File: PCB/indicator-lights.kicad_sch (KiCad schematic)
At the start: 10 parts, among them IC9 IS31FL3218-GRLS2

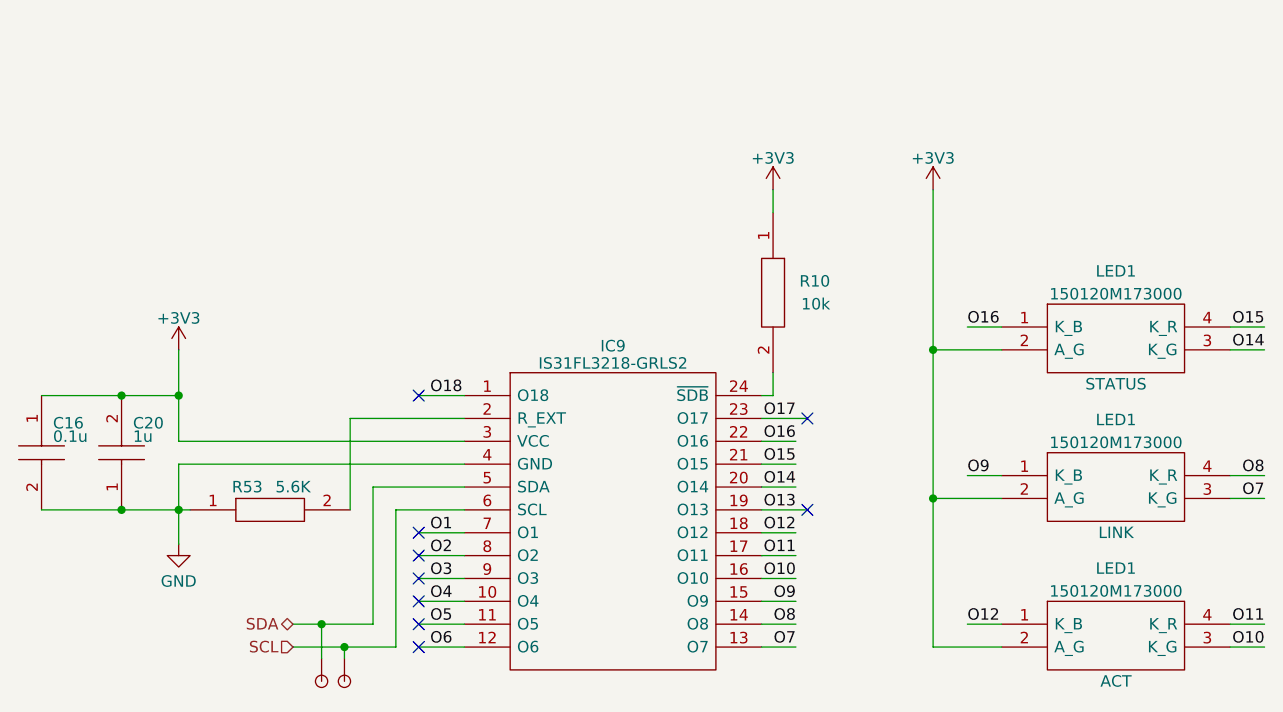
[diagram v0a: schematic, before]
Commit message: preliminary routing completed
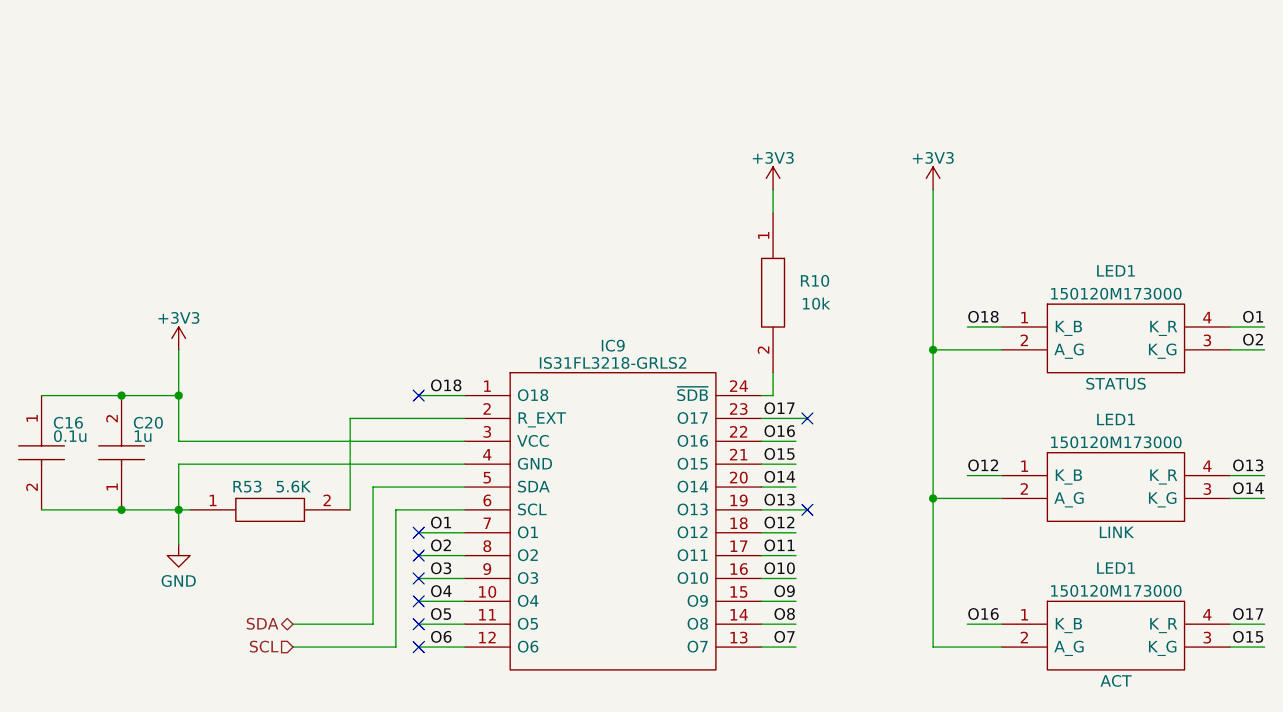
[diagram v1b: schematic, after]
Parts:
- removed DBG5 (x2): ~, Oro Footprints:DebugPin, symbol Oro:DebugPin
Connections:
- net O1: now also LED1.4 (K_R)
- net O10: no longer LED1.3 (K_G)
- net O11: no longer LED1.4 (K_R)
- net O12: now also LED1.1 (K_B); no longer LED1.1 (K_B)
- net O13: now also LED1.4 (K_R)
- net O14: now also LED1.3 (K_G); no longer LED1.3 (K_G)
- net O15: now also LED1.3 (K_G); no longer LED1.4 (K_R)
- net O16: now also LED1.1 (K_B); no longer LED1.1 (K_B)
- net O17: now also LED1.4 (K_R)
- net O18: now also LED1.1 (K_B)
- net O2: now also LED1.3 (K_G)
- net O7: no longer LED1.3 (K_G)
- net O8: no longer LED1.4 (K_R)
- net O9: no longer LED1.1 (K_B)
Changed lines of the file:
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@@
   (junction (at 87.63 96.52) (diameter 0) (color 0 0 0 0)
   )
-  (junction (at 103.505 121.92) (diameter 0) (color 0 0 0 0)
-  )
   (junction (at 81.28 109.22) (diameter 0) (color 0 0 0 0)
   )
   (junction (at 171.45 91.44) (diameter 0) (color 0 0 0 0)
-  )
-  (junction (at 106.045 124.46) (diameter 0) (color 0 0 0 0)
   )
   (junction (at 87.63 109.22) (diameter 0) (color 0 0 0 0)
@@
     (stroke (width 0) (type default))
   )
-  (wire (pts (xy 100.33 121.92) (xy 103.505 121.92))
+  (wire (pts (xy 100.33 121.92) (xy 109.22 121.92))
     (stroke (width 0) (type default))
   )
@@
     (stroke (width 0) (type default))
   )
-  (wire (pts (xy 103.505 121.92) (xy 109.22 121.92))
-    (stroke (width 0) (type default))
-  )
   (wire (pts (xy 208.28 124.46) (xy 204.47 124.46))
     (stroke (width 0) (type default))
@@
     (stroke (width 0) (type default))
   )
-  (wire (pts (xy 103.505 121.92) (xy 103.505 125.73))
-    (stroke (width 0) (type default))
-  )
   (wire (pts (xy 156.21 119.38) (xy 152.4 119.38))
     (stroke (width 0) (type default))
@@
     (stroke (width 0) (type default))
   )
-  (wire (pts (xy 106.045 124.46) (xy 111.76 124.46))
-    (stroke (width 0) (type default))
-  )
   (wire (pts (xy 114.3 111.76) (xy 119.38 111.76))
     (stroke (width 0) (type default))
@@
     (stroke (width 0) (type default))
   )
-  (wire (pts (xy 106.045 124.46) (xy 106.045 125.73))
-    (stroke (width 0) (type default))
-  )
   (wire (pts (xy 72.39 109.22) (xy 81.28 109.22))
     (stroke (width 0) (type default))
@@
     (stroke (width 0) (type default))
   )
-  (wire (pts (xy 100.33 124.46) (xy 106.045 124.46))
+  (wire (pts (xy 100.33 124.46) (xy 111.76 124.46))
     (stroke (width 0) (type default))
   )
@@
     (effects (font (size 1.27 1.27)) (justify left bottom))
   )
-  (label "O14" (at 208.28 91.44 180) (fields_autoplaced)
-    (effects (font (size 1.27 1.27)) (justify right bottom))
-  )
-  (label "O16" (at 175.26 88.9 0) (fields_autoplaced)
+  (label "O2" (at 208.28 91.44 180) (fields_autoplaced)
+    (effects (font (size 1.27 1.27)) (justify right bottom))
+  )
+  (label "O18" (at 175.26 88.9 0) (fields_autoplaced)
     (effects (font (size 1.27 1.27)) (justify left bottom))
   )
@@
     (effects (font (size 1.27 1.27)) (justify left bottom))
   )
-  (label "O15" (at 208.28 88.9 180) (fields_autoplaced)
+  (label "O1" (at 208.28 88.9 180) (fields_autoplaced)
     (effects (font (size 1.27 1.27)) (justify right bottom))
   )
@@
     (effects (font (size 1.27 1.27)) (justify left bottom))
   )
-  (label "O11" (at 208.28 121.92 180) (fields_autoplaced)
-    (effects (font (size 1.27 1.27)) (justify right bottom))
-  )
-  (label "O12" (at 175.26 121.92 0) (fields_autoplaced)
-    (effects (font (size 1.27 1.27)) (justify left bottom))
-  )
-  (label "O10" (at 208.28 124.46 180) (fields_autoplaced)
+  (label "O17" (at 208.28 121.92 180) (fields_autoplaced)
+    (effects (font (size 1.27 1.27)) (justify right bottom))
+  )
+  (label "O16" (at 175.26 121.92 0) (fields_autoplaced)
+    (effects (font (size 1.27 1.27)) (justify left bottom))
+  )
+  (label "O15" (at 208.28 124.46 180) (fields_autoplaced)
     (effects (font (size 1.27 1.27)) (justify right bottom))
   )
@@
     (effects (font (size 1.27 1.27)) (justify right bottom))
   )
-  (label "O7" (at 208.28 107.95 180) (fields_autoplaced)
+  (label "O14" (at 208.28 107.95 180) (fields_autoplaced)
     (effects (font (size 1.27 1.27)) (justify right bottom))
   )
@@
     (effects (font (size 1.27 1.27)) (justify right bottom))
   )
-  (label "O8" (at 208.28 105.41 180) (fields_autoplaced)
-    (effects (font (size 1.27 1.27)) (justify right bottom))
-  )
-  (label "O9" (at 175.26 105.41 0) (fields_autoplaced)
-    (effects (font (size 1.27 1.27)) (justify left bottom))
+  (label "O12" (at 175.26 105.41 0) (fields_autoplaced)
+    (effects (font (size 1.27 1.27)) (justify left bottom))
+  )
+  (label "O13" (at 208.28 105.41 180) (fields_autoplaced)
+    (effects (font (size 1.27 1.27)) (justify right bottom))
   )
   (label "O10" (at 156.21 116.84 180) (fields_autoplaced)
@@
     )
   )
-  (symbol (lib_id "Oro:DebugPin") (at 103.505 125.73 270) (unit 1)
-    (in_bom no) (on_board yes) (dnp no)
-    (property "Reference" "DBG5" (at 103.505 131.445 0)
-      (effects (font (size 1.27 1.27)) hide)
-    )
-    (property "Value" "~" (at 103.505 125.73 0)
-      (effects (font (size 1.27 1.27)) hide)
-    )
-    (property "Footprint" "Oro Footprints:DebugPin" (at 106.045 127 0)
-      (effects (font (size 1.27 1.27)) hide)
-    )
-    (property "Datasheet" "" (at 103.505 125.73 0)
-      (effects (font (size 1.27 1.27)) hide)
-    )
-    (property "Sim.Enable" "0" (at 106.045 139.7 0)
-      (effects (font (size 1.27 1.27)) hide)
-    )
-    (pin "1")
-    (instances
-      (project "OroLink"
-        (path "/e89dcd22-1250-4a5b-b778-1c95a0dd623d/f955395e-bf1a-4ef3-9cfe-ec9d49f66988"
-          (reference "DBG5") (unit 1)
-        )
-        (path "/e89dcd22-1250-4a5b-b778-1c95a0dd623d/1b3eede1-74b0-4c0b-b4f1-7ec1bfc1f54f"
-          (reference "DBG16") (unit 1)
-        )
-        (path "/e89dcd22-1250-4a5b-b778-1c95a0dd623d/52771c01-2e58-4900-abe5-411f688d020f"
-          (reference "DBG25") (unit 1)
-        )
-        (path "/e89dcd22-1250-4a5b-b778-1c95a0dd623d/7cebe953-3148-4b67-a6c9-1f2594261687"
-          (reference "DBG26") (unit 1)
-        )
-        (path "/e89dcd22-1250-4a5b-b778-1c95a0dd623d/49c51f54-e113-47ff-b1ad-86c9ad73cafa"
-          (reference "DBG31") (unit 1)
-        )
-      )
-    )
-  )
   (symbol (lib_id "SamacSys_Parts:RK73H1ETTP1002F") (at 153.67 76.2 270) (unit 1)
     (in_bom yes) (on_board yes) (dnp no)
@@
         )
       )
-    )
-  )
-  (symbol (lib_id "Oro:DebugPin") (at 106.045 125.73 270) (unit 1)
-    (in_bom no) (on_board yes) (dnp no)
-    (property "Reference" "DBG5" (at 106.045 131.445 0)
-      (effects (font (size 1.27 1.27)) hide)
-    )
-    (property "Value" "~" (at 106.045 125.73 0)
-      (effects (font (size 1.27 1.27)) hide)
-    )
-    (property "Footprint" "Oro Footprints:DebugPin" (at 108.585 127 0)
-      (effects (font (size 1.27 1.27)) hide)
-    )
-    (property "Datasheet" "" (at 106.045 125.73 0)
-      (effects (font (size 1.27 1.27)) hide)
-    )
-    (property "Sim.Enable" "0" (at 108.585 139.7 0)
-      (effects (font (size 1.27 1.27)) hide)
-    )
-    (pin "1")
-    (instances
-      (project "OroLink"
-        (path "/e89dcd22-1250-4a5b-b778-1c95a0dd623d/f955395e-bf1a-4ef3-9cfe-ec9d49f66988"
-          (reference "DBG5") (unit 1)
-        )
-        (path "/e89dcd22-1250-4a5b-b778-1c95a0dd623d/1b3eede1-74b0-4c0b-b4f1-7ec1bfc1f54f"
-          (reference "DBG16") (unit 1)
-        )
-        (path "/e89dcd22-1250-4a5b-b778-1c95a0dd623d/52771c01-2e58-4900-abe5-411f688d020f"
-          (reference "DBG25") (unit 1)
-        )
-        (path "/e89dcd22-1250-4a5b-b778-1c95a0dd623d/7cebe953-3148-4b67-a6c9-1f2594261687"
-          (reference "DBG26") (unit 1)
-        )
-        (path "/e89dcd22-1250-4a5b-b778-1c95a0dd623d/49c51f54-e113-47ff-b1ad-86c9ad73cafa"
-          (reference "DBG32") (unit 1)
-        )
-      )

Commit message: fix mouser ID on MSAST1L3YB5104KFNA01 caps
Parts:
- C16: symbol SamacSys_Parts:MSAST1L3YB5104KFNA01 -> Oro:MSAST1L3YB5104KFNA01; Mouser Part Number (none) -> 963-MSAST1L3YB5104KF; Mouser Price/Stock (none) -> https://www.mouser.de/ProductDetail/TAIYO-YUDEN/MSAST1L3YB5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
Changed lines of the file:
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@@
     )
   )
-  (symbol (lib_id "SamacSys_Parts:MSAST1L3YB5104KFNA01") (at 72.39 96.52 90) (mirror x) (unit 1)
+  (symbol (lib_id "Oro:MSAST1L3YB5104KFNA01") (at 72.39 96.52 90) (mirror x) (unit 1)
     (in_bom yes) (on_board yes) (dnp no)
     (property "Reference" "C16" (at 73.66 100.33 90)
@@
       (effects (font (size 1.27 1.27)) (justify left) hide)
     )
-    (property "Mouser Part Number" "" (at 86.36 105.41 0)
+    (property "Mouser Part Number" "963-MSAST1L3YB5104KF" (at 86.36 105.41 0)
       (effects (font (size 1.27 1.27)) (justify left) hide)
     )
-    (property "Mouser Price/Stock" "" (at 88.9 105.41 0)
+    (property "Mouser Price/Stock" "https://www.mouser.de/ProductDetail/TAIYO-YUDEN/MSAST1L3YB5104KFNA01?qs=tlsG%2FOw5FFhBwK%252BMwEZpCA%3D%3D" (at 88.9 105.41 0)
       (effects (font (size 1.27 1.27)) (justify left) hide)
     )

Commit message: fix remaining missing mouser ID BOM entries
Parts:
- R53: symbol SamacSys_Parts:CRGP0402F5K6 -> Oro:CRGP0402F5K6; Mouser Part Number (none) -> 279-CRGP0402F5K6; Mouser Price/Stock (none) -> https://www.mouser.de/ProductDetail/TE-Connectivity-Holswor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
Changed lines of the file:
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@@
     )
   )
-  (symbol (lib_id "SamacSys_Parts:CRGP0402F5K6") (at 88.9 109.22 0) (unit 1)
+  (symbol (lib_id "Oro:CRGP0402F5K6") (at 88.9 109.22 0) (unit 1)
     (in_bom yes) (on_board yes) (dnp no)
     (property "Reference" "R53" (at 95.25 106.68 0)
@@
       (effects (font (size 1.27 1.27)) (justify left) hide)
     )
-    (property "Mouser Part Number" "" (at 102.87 123.19 0)
+    (property "Mouser Part Number" "279-CRGP0402F5K6" (at 102.87 123.19 0)
       (effects (font (size 1.27 1.27)) (justify left) hide)
     )
-    (property "Mouser Price/Stock" "" (at 102.87 125.73 0)
+    (property "Mouser Price/Stock" "https://www.mouser.de/ProductDetail/TE-Connectivity-Holsworthy/CRGP0402F5K6?qs=wUXugUrL1qxVwNCmbd06hg%3D%3D" (at 102.87 125.73 0)
       (effects (font (size 1.27 1.27)) (justify left) hide)
     )

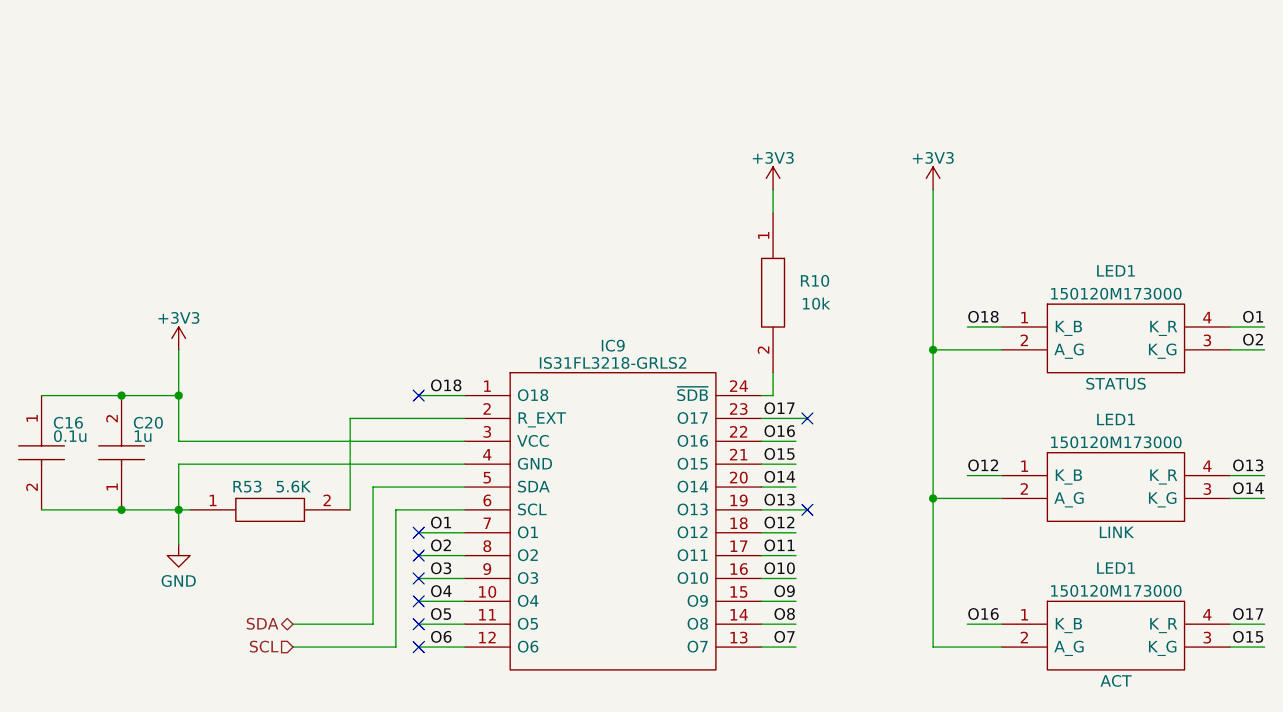
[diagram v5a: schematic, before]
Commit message: put all components behind MOSFETs (closes #39)
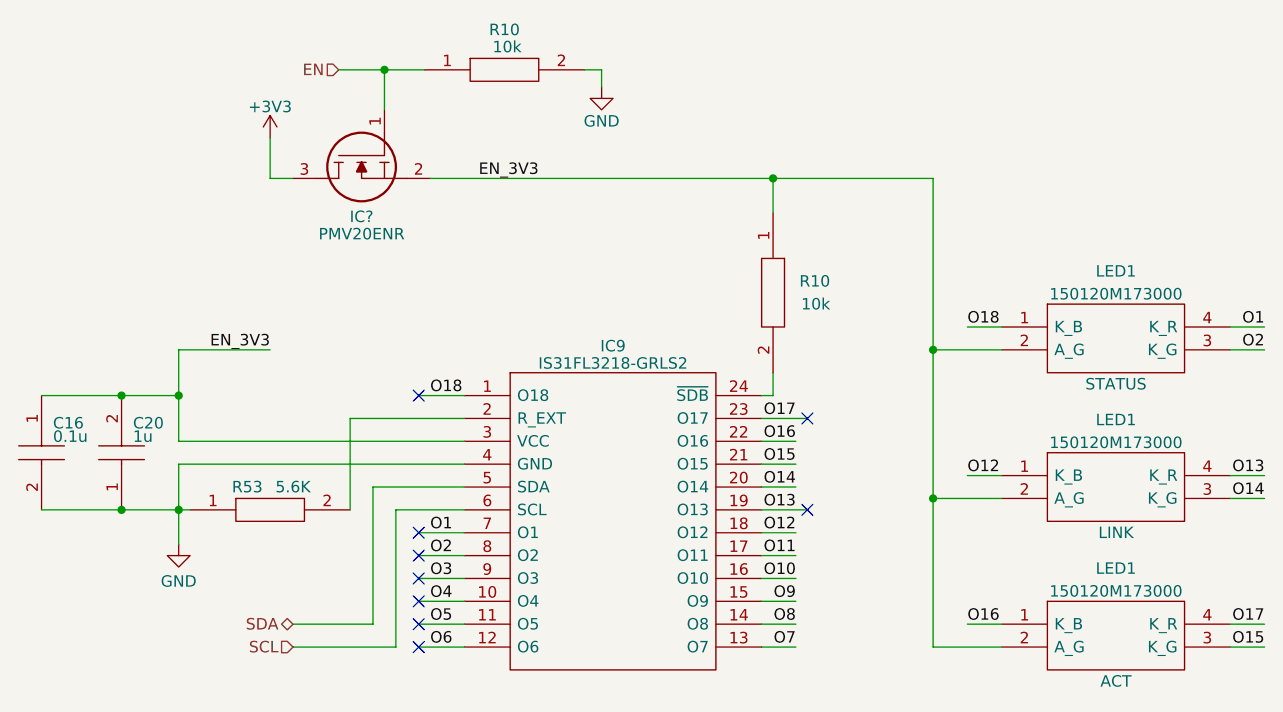
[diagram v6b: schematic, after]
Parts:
- added IC?: PMV20ENR, SamacSys_Parts:SOT95P230X110-3N, symbol SamacSys_Parts:CSD13380F3T
- added R10: 10k, RESC1005X40N, symbol SamacSys_Parts:RK73H1ETTP1002F
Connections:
- net +3V3: now also IC?.3; no longer C16.1, C20.2, IC9.3 (VCC), LED1.2 (A_G), LED1.2 (A_G), LED1.2 (A_G), R10.1
- net GND: now also R10.2
- new net EN: IC?.1, R10.1
- new net EN_3V3: C16.1, C20.2, IC9.3 (VCC), IC?.2, LED1.2 (A_G), LED1.2 (A_G), LED1.2 (A_G), R10.1
